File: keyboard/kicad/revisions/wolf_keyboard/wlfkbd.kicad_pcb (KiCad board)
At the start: 2 copper layers, 289.7 x 109.2 mm, 214 parts, among them Q1 AO3400A, Q2 AO3407A, Q3_R1 AO3407A, Q4_R1 AO3400A, SW1 SW_Push, SW10 SW_Push, SW11 SW_Push, SW12 SW_Push, SW13 SW_Push, SW14 SW_Push, SW15 SW_Push, SW16 SW_Push, SW17 SW_Push, SW18 SW_Push, SW19 SW_Push, SW2 SW_Push, SW20 SW_Push, SW21 SW_Push, SW22 SW_Push, SW23 SW_Push, SW24 SW_Push, SW25 SW_Push, SW26 SW_Push, SW27 SW_Push, SW28 SW_Push, SW29 SW_Push, SW3 SW_Push, SW30 SW_Push, SW31 SW_Push, SW32 SW_Push, SW33 SW_Push, SW34 SW_Push, SW35 SW_Push, SW36 SW_Push, SW37 SW_Push, SW38 SW_Push, SW39 SW_Push, SW4 SW_Push, SW40 SW_Push, SW5 SW_Push, SW6 SW_Push, SW7 SW_Push, SW8 SW_Push, SW9 SW_Push, U1 XIAO-nRF52840-SMD, U3 XIAO-nRF52840-SMD

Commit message: refactor: improve traces routing
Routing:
- net Net-(D22-DOUT): track 21.8 -> 14.8 mm, vias 3 -> 2
- net Net-(D23-DOUT): track 19.3 -> 16.0 mm
- net ROW0: track 133.6 -> 132.6 mm
- net ROW2_R: track 189.7 -> 190.3 mm

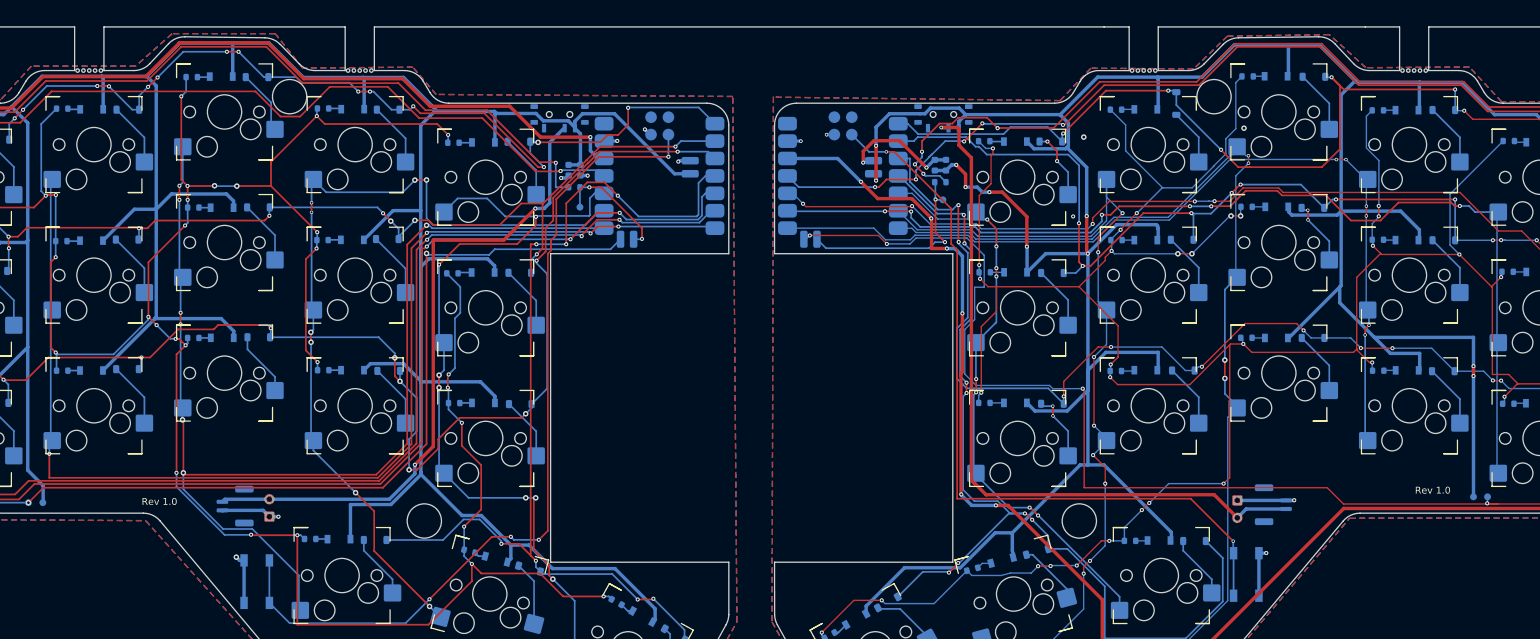
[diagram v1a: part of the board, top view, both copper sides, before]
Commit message: refactor: fix minor DRC issues
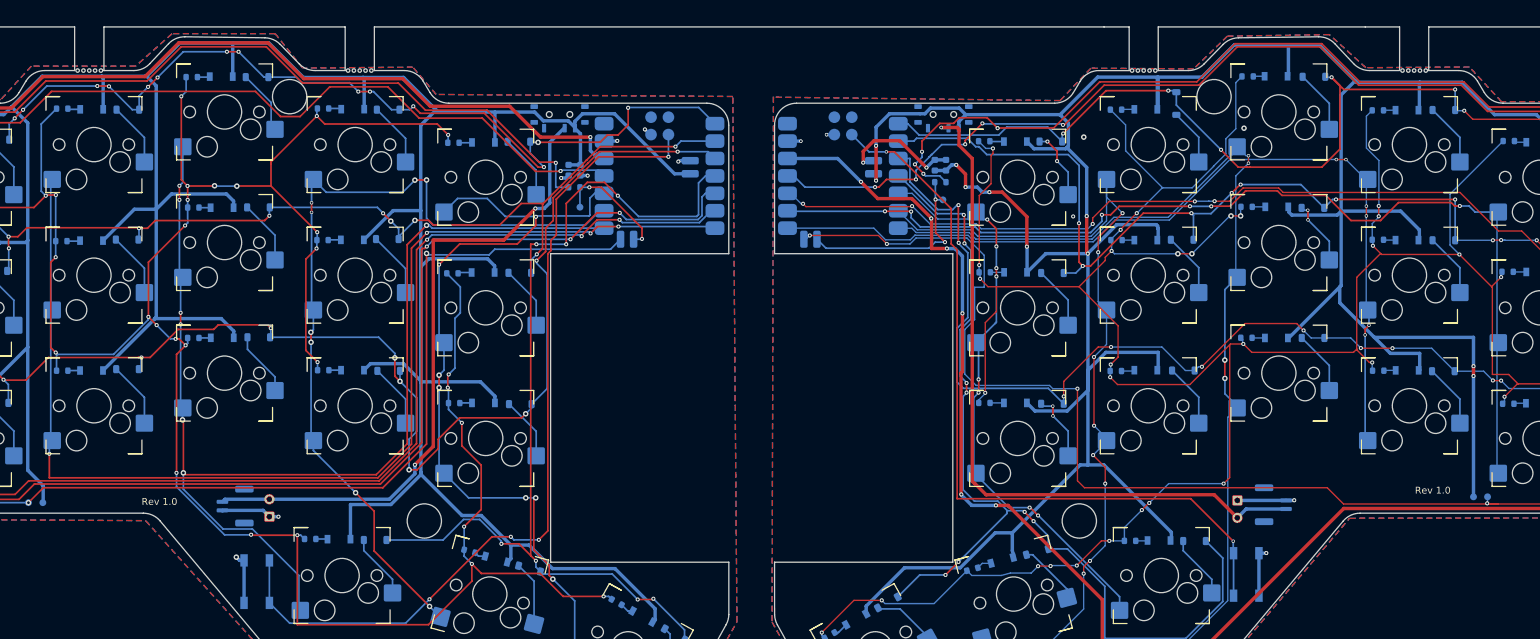
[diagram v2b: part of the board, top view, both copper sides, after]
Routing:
- net VBAT_R: track 542.6 -> 547.0 mm
- net ROW3_R: track 142.0 -> 139.9 mm
